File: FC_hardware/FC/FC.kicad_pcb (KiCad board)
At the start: 4 copper layers, 34 x 34 mm, 86 parts, among them J1 Pin_01x04, J10 GND, J11 GND, J12 GND, J13 530481410, J15 Pin_01x03, J16 PB2, J17 PC9, J18 PC8, J19 PB7, J2 USB4105GFA120, J20 PB6, J21 PA8, J22 PC11, J23 PC10, J24 PC12, J25 PB10, J26 PC7, J27 PC6, J3 530480810, J4 BAT, J5 5V, J6 5V, J7 3V3, J8 3V3, J9 GND, Q1 BC807W, U1 MP2348, U2 AMS1117-3.3, U3 STM32F446RETx, U4 MPU-9250, U5 DPS368XTSA1, U6 USBLC6-2SC6, Y1 ABM8G-25MHZ

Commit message: Dump pcb design
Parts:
- removed J17: PC9, footprints:1.27mm_pin
- removed J26: PC7, footprints:1.27mm_pin
- removed J27: PC6, footprints:1.27mm_pin
- removed J3: 530480810, footprints:MOLEX_530480810
- removed JP1: BOOT0, Jumper:SolderJumper-2_P1.3mm_Bridged_RoundedPad1.0x1.5mm
- added C23: 10nF, Capacitor_SMD:C_0603_1608Metric, F.Cu at (111.3, 108.5)
- added C24: 10uF, Capacitor_SMD:C_0603_1608Metric, F.Cu at (109.2, 104.5)
- added C25: 10uF, Capacitor_SMD:C_0603_1608Metric, F.Cu at (106.2, 104.5)
- added FB1: 120R, Inductor_SMD:L_1206_3216Metric, F.Cu at (108.2, 106.5)
- added J14: PB10, footprints:1.27mm_pin, F.Cu at (118.6, 129.2)
- C1, C2, C6, F1, J2, L1, Q1, R11, R13, R18, S1, U6: moved to B.Cu
- C10: value 6.8pF -> 47uF; footprint Capacitor_SMD:C_0603_1608Metric -> Capacitor_Tantalum_SMD:CP_EIA-3528-12_Kemet-T; moved to B.Cu
- C11, C12: value 0.1uF -> 6.8pF
- C15: value 0.1uF -> 1uF; footprint Capacitor_SMD:C_0603_1608Metric -> Capacitor_SMD:C_0805_2012Metric
- C3: value 6.8nF -> 47uF; footprint Capacitor_SMD:C_0603_1608Metric -> Capacitor_Tantalum_SMD:CP_EIA-3528-12_Kemet-T; moved to B.Cu
- C4, C5: value 47uF -> 0.1uF; footprint Capacitor_Tantalum_SMD:CP_EIA-3528-12_Kemet-T -> Capacitor_SMD:C_0603_1608Metric
- C7: value 1uF -> 0.1uF; footprint Capacitor_SMD:C_0805_2012Metric -> Capacitor_SMD:C_0603_1608Metric; moved to B.Cu
- C8: value 1uF -> 6.8nF; footprint Capacitor_SMD:C_0805_2012Metric -> Capacitor_SMD:C_0603_1608Metric; moved to B.Cu
- C9: value 6.8pF -> 1uF; footprint Capacitor_SMD:C_0603_1608Metric -> Capacitor_SMD:C_0805_2012Metric; moved to B.Cu
- D1: value B320 -> Power-Red; footprint Diode_SMD:D_SMA -> LED_SMD:LED_0805_2012Metric
- D2: value Power-Red -> Status-Green
- D3: value Status-Green -> B320; footprint LED_SMD:LED_0805_2012Metric -> Diode_SMD:D_SMA; moved to B.Cu
- H1, H2, H3, H4: footprint MountingHole:MountingHole_2.2mm_M2 -> MountingHole:MountingHole_3.2mm_M3
- J1: value Pin_01x04 -> Conn_01x14; footprint Connector_PinHeader_1.27mm:PinHeader_1x04_P1.27mm_Vertical -> Connector_JST:JST_SH_SM14B-SRSS-TB_1x14-1MP_P1.00mm_Horizontal
- J10: value GND -> BAT; footprint footprints:1.27mm_pin -> Connector_PinHeader_2.00mm:PinHeader_1x01_P2.00mm_Vertical
- J11, J12: value GND -> 5V
- J13: value 530481410 -> PC12; footprint footprints:MOLEX_530481410 -> footprints:1.27mm_pin
- J15: value Pin_01x03 -> PC7; footprint Connector_PinHeader_1.27mm:PinHeader_1x03_P1.27mm_Vertical -> footprints:1.27mm_pin
- J16: value PB2 -> PC6
- J18: value PC8 -> 3V3
- J19: value PB7 -> 3V3
- J20: value PB6 -> GND
- J21: value PA8 -> GND
- J22: value PC11 -> GND
- J23: value PC10 -> GND
- J24: value PC12 -> SM08B-SRSS-TB; footprint footprints:1.27mm_pin -> Connector_JST:JST_SH_SM08B-SRSS-TB_1x08-1MP_P1.00mm_Horizontal
- J25: value PB10 -> Conn_01x06; footprint footprints:1.27mm_pin -> Connector_PinHeader_1.27mm:PinHeader_1x06_P1.27mm_Vertical; moved to B.Cu
- J4: value BAT -> PA8
- J5: value 5V -> PB6
- J6: value 5V -> PB7
- J7: value 3V3 -> PC8
- J8: value 3V3 -> PC9
- J9: value GND -> PC9
- JP2: value ESC_TEL -> BOOT0; footprint Jumper:SolderJumper-2_P1.3mm_Open_RoundedPad1.0x1.5mm -> Jumper:SolderJumper-2_P1.3mm_Bridged_RoundedPad1.0x1.5mm; moved to B.Cu
- R1: value 40.2k -> 604k
- R10: value 1k -> 4.7k; moved to B.Cu
- R12: value 40.2k -> 4.7k; moved to B.Cu
- R14: value 1k -> 5.1k
- R15: value 4.7k -> 1k; moved to B.Cu
- R16: value 4.7k -> 40.2k
- R17: value 1k -> 4.7k
- R2: value 7.68k -> 1k
- R3: value 15k -> 20R; moved to B.Cu
- R4: value 20R -> 15k; moved to B.Cu
- R5: value 604k -> 40.2k; moved to B.Cu
- R6: value 4.7k -> 7.68k; moved to B.Cu
- R7: value 4.7k -> 5.1k
- R8: value 5.1k -> 1k
- R9: value 5.1k -> 4.7k; moved to B.Cu
- U1: value MP2348 -> AMS1117-3.3; footprint Package_TO_SOT_SMD:SOT-583-8 -> Package_TO_SOT_SMD:SOT-223-3_TabPin2; moved to B.Cu
- U2: value AMS1117-3.3 -> MPU-9250; footprint Package_TO_SOT_SMD:SOT-223-3_TabPin2 -> Sensor_Motion:InvenSense_QFN-24_3x3mm_P0.4mm
- U3: value STM32F446RETx -> MP2348; footprint Package_QFP:LQFP-64_10x10mm_P0.5mm -> Package_TO_SOT_SMD:SOT-583-8; moved to B.Cu
- U4: value MPU-9250 -> DPS368XTSA1; footprint Sensor_Motion:InvenSense_QFN-24_3x3mm_P0.4mm -> footprints:XDCR_DPS368XTSA1; moved to B.Cu
- U5: value DPS368XTSA1 -> STM32F446RETx; footprint footprints:XDCR_DPS368XTSA1 -> Package_QFP:LQFP-64_10x10mm_P0.5mm
- moved J13 90.0 mm to (117.3, 129.2)
- moved C19 83.3 mm to (117.1, 123.7)
- moved C3 82.0 mm to (116.7, 116.2), turned to 180 degrees
- moved R13 81.0 mm to (124.2, 116.5)
- moved C4 80.4 mm to (109.8, 127.2), turned to -90 degrees
- moved C17 78.1 mm to (120.2, 112.3), turned to 90 degrees
- moved S1 77.1 mm to (105.8, 127.6), turned to 180 degrees
- moved R15 76.6 mm to (115.9, 118.8)
- moved J1 74.7 mm to (127.0, 113.0), turned to 90 degrees
- moved C5 73.1 mm to (110.8, 124.3), turned to 180 degrees
- moved C18 73.0 mm to (118.4, 110.0), turned to 180 degrees
- moved R4 72.4 mm to (103.8, 110.3)
- moved R10 72.1 mm to (107.0, 124.8), turned to 180 degrees
- moved R5 69.0 mm to (110.0, 108.8), turned to -90 degrees
- moved C20 68.2 mm to (105.0, 113.2), turned to -90 degrees
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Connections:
- C10 pad 1: /OSC_OUT -> +5V
- C11 pad 2: +3V3 -> /RCC_OSC_IN
- C12 pad 1: +3V3 -> /RCC_OSC_OUT
- C13 pad 1: Net-(U4-REGOUT) -> +5V
- C14 pad 1: +5V -> +3V3
- C15 pad 2: +3V3 -> /VCAP_1
- C16 pad 1: /ADC_I -> GND
- C16 pad 2: GND -> +3V3
- C17 pad 1: /ADC_U -> GND
- C17 pad 2: GND -> +3V3
- C2 pad 1: +5V -> +3V3
- C21 pad 1: GND -> /VBAT_ADC
- C21 pad 2: +3V3 -> GND
- C22 pad 1: +3V3 -> /IBAT_ADC
- C3 pad 1: Net-(U1-SS) -> +3V3
- C4 pad 1: +5V -> +3V3
- C5 pad 1: +3V3 -> Net-(U2-REGOUT)
- C7 pad 1: +3V3 -> GND
- C7 pad 2: GND -> +3V3
- C8 pad 1: GND -> Net-(U3-SS)
- C8 pad 2: /VCAP_1 -> GND
- C9 pad 1: GND -> +5V
- C9 pad 2: /OSC_IN -> GND
- D1 pad 1: +5V -> Net-(D1-K)
- D1 pad 2: VBUS -> +3V3
- D2 pad 1: Net-(D2-K) -> GND
- D2 pad 2: +3V3 -> Net-(D2-A)
- D3 pad 1: Net-(D3-K) -> +5V
- D3 pad 2: /LED -> VBUS
- J1 pad 1: GND -> unconnected-(J1-Pin_1-Pad1)
- J1 pad 2: /SWCLK -> /GPS_TX
- J1 pad 3: /SWDIO -> /GPS_RX
- J1 pad 4: +3V3 -> Net-(J1-Pin_4)
- J10 pad 1: GND -> +BATT
- J11 pad 1: GND -> +5V
- J12 pad 1: GND -> +5V
- J13 pad 1: GND -> /GEN_I2C3_SDA
- J15 pad 1: GND -> /GEN_UART2_RX
- J16 pad 1: /GEN_MOSI -> /GEN_UART2_TX
- J18 pad 1: /TIM8_3 -> +3V3
- J19 pad 1: /TIM4_2 -> +3V3
- J20 pad 1: /TIM4_1 -> GND
- J21 pad 1: /TIM1_1 -> GND
- J22 pad 1: /GEN_MISO -> GND
- J23 pad 1: /GEN_SCK -> GND
- J24 pad 1: /GEN_SDA -> GND
- J25 pad 1: /GEN_SCL -> GND
- J4 pad 1: +BATT -> /GEN_TIM2_CH1
- J5 pad 1: +5V -> /GEN_TIM2_CH2
- J6 pad 1: +5V -> /GEN_TIM2_CH3
- J7 pad 1: +3V3 -> /GEN_TIM2_CH4
- J8 pad 1: +3V3 -> /GEN_TIM8_CH3
- J9 pad 1: GND -> /GEN_TIM10_CH1
- JP2 pad 1: /ESC_RX -> GND
- JP2 pad 2: /ESC_RX_MCU -> /BOOT
- R1 pad 1: +5V -> /BAT_VIN
- R1 pad 2: Net-(R1-Pad2) -> Net-(U3-EN)
- R10 pad 1: /ADC_I -> /NRST
- R10 pad 2: Net-(J3-CURR) -> +3V3
- R11 pad 1: GND -> +3V3
- R11 pad 2: /ADC_U -> /MAG_SDA
- R12 pad 1: +BATT -> /BOOT
- R12 pad 2: /ADC_U -> +3V3
- R13 pad 1: GND -> Net-(Q1-B)
- R13 pad 2: Net-(D2-K) -> Net-(J1-Pin_4)
- R14 pad 1: GND -> Net-(J2-CC2)
- R14 pad 2: Net-(D3-K) -> GND
- R15 pad 1: /MAG_SDA -> GND
- R15 pad 2: +3V3 -> /SBUS_RX
- R16 pad 1: /MAG_SCL -> +BATT
- R16 pad 2: +3V3 -> /VBAT_ADC
- R17 pad 2: /SBUS_RX -> /VBAT_ADC
- R18 pad 1: Net-(Q1-B) -> /IBAT_ADC
- R18 pad 2: Net-(J13-SBUS_RX) -> Net-(J24-Pad7)
- R2 pad 1: Net-(R1-Pad2) -> GND
- R2 pad 2: GND -> Net-(D1-K)
- R3 pad 1: Net-(U1-FB) -> Net-(U3-BST)
- R3 pad 2: Net-(R1-Pad2) -> Net-(C6-Pad1)
- R4 pad 1: Net-(U1-BST) -> Net-(U3-FB)
- R4 pad 2: Net-(C6-Pad1) -> Net-(R4-Pad2)
- R5 pad 1: /BAT_VIN -> +5V
- R5 pad 2: Net-(U1-EN) -> Net-(R4-Pad2)
- R6 pad 1: /NRST -> Net-(R4-Pad2)
- R6 pad 2: +3V3 -> GND
- R7 pad 1: /BOOT -> Net-(J2-CC1)
- R7 pad 2: +3V3 -> GND
- R8 pad 1: Net-(J2-CC2) -> /STATUS_LED
- R8 pad 2: GND -> Net-(D2-A)
- R9 pad 1: Net-(J2-CC1) -> /MAG_SCL
- R9 pad 2: GND -> +3V3
- U1 pad 1: unconnected-(U1-MODE-Pad1) -> GND
- U1 pad 2: /BAT_VIN -> +3V3
- U1 pad 3: /SW -> +5V
- U2 pad 1: GND -> +3V3
- U2 pad 2: +3V3 -> (no net)
- U2 pad 3: +5V -> (no net)
- U3 pad 1: +3V3 -> unconnected-(U3-MODE-Pad1)
- U3 pad 2: /BAR_CSB -> /BAT_VIN
- U3 pad 3: unconnected-(U3-PC14-Pad3) -> /SW
- U3 pad 4: unconnected-(U3-PC15-Pad4) -> GND
- U3 pad 5: /OSC_IN -> Net-(U3-BST)
- U3 pad 6: /OSC_OUT -> Net-(U3-EN)
- U3 pad 7: /NRST -> Net-(U3-SS)
- U3 pad 8: /ADC_I -> Net-(U3-FB)
- U4 pad 1: +3V3 -> GND
- U4 pad 2: (no net) -> /BAR_CS
- U4 pad 3: (no net) -> /IMU_BAR_MOSI
- U4 pad 4: (no net) -> /IMU_BAR_SCK
- U4 pad 5: (no net) -> /IMU_BAR_MISO
- U4 pad 6: (no net) -> +3V3
- U4 pad 7: unconnected-(U4-AUX_CL-Pad7) -> GND
- U5 pad 1: GND -> +3V3
- U5 pad 2: /BAR_CSB -> /LORA_IRQN
- U5 pad 3: /IMU_BAR_MOSI -> /LORA_RST
- U5 pad 4: /IMU_BAR_SCK -> unconnected-(U5-PC15-Pad4)
- U5 pad 5: /IMU_BAR_MISO -> /RCC_OSC_IN
- U5 pad 6: +3V3 -> /RCC_OSC_OUT
- U5 pad 7: GND -> /NRST
- U5 pad 8: +3V3 -> unconnected-(U5-PC0-Pad8)
- U6 pad 1: /USB_DP -> /USB_OTG_FS_DP
- U6 pad 3: /USB_DN -> /USB_OTG_FS_DN
- Y1 pad 1: /OSC_IN -> /RCC_OSC_IN
- Y1 pad 3: /OSC_OUT -> /RCC_OSC_OUT
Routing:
- net GND: track 0.00 -> 58.9 mm, vias 0 -> 48
- net /USB_OTG_FS_DP: track 0.00 -> 35.3 mm, vias 0 -> 1
- net /USB_OTG_FS_DN: track 0.00 -> 35.3 mm, vias 0 -> 1
- net +3V3: track 0.00 -> 28.1 mm, vias 0 -> 26
- net /NRST: track 0.00 -> 24.7 mm, vias 0 -> 1
- net +5V: track 0.00 -> 19.7 mm, vias 0 -> 2
- net +BATT: track 0.00 -> 18.0 mm, vias 0 -> 2
- net /GEN_TIM10_CH1: track 0.00 -> 17.8 mm, vias 0 -> 2
- net /GEN_TIM2_CH2: track 0.00 -> 17.7 mm, vias 0 -> 2
- net /STATUS_LED: track 0.00 -> 16.7 mm
- net /GEN_UART2_TX: track 0.00 -> 16.7 mm
- net /IBAT_ADC: track 0.00 -> 16.3 mm, vias 0 -> 1
- net /IMU_BAR_SCK: track 0.00 -> 16.1 mm, vias 0 -> 1
- net /GEN_TIM2_CH3: track 0.00 -> 15.4 mm, vias 0 -> 1
- net /GEN_UART2_RX: track 0.00 -> 15.3 mm, vias 0 -> 2
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- added copper zone on B.Cu, net +3V3
- added copper zone on In1.Cu, net +3V3
- added copper zone on B.Cu, net +5V
- added copper zone on B.Cu, net /SW
- added copper zone on B.Cu, net GND
- added copper zone on In2.Cu, net GND
- added copper zone on B.Cu, net VBUS
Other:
- board size 34 x 34 mm -> 35 x 35 mm

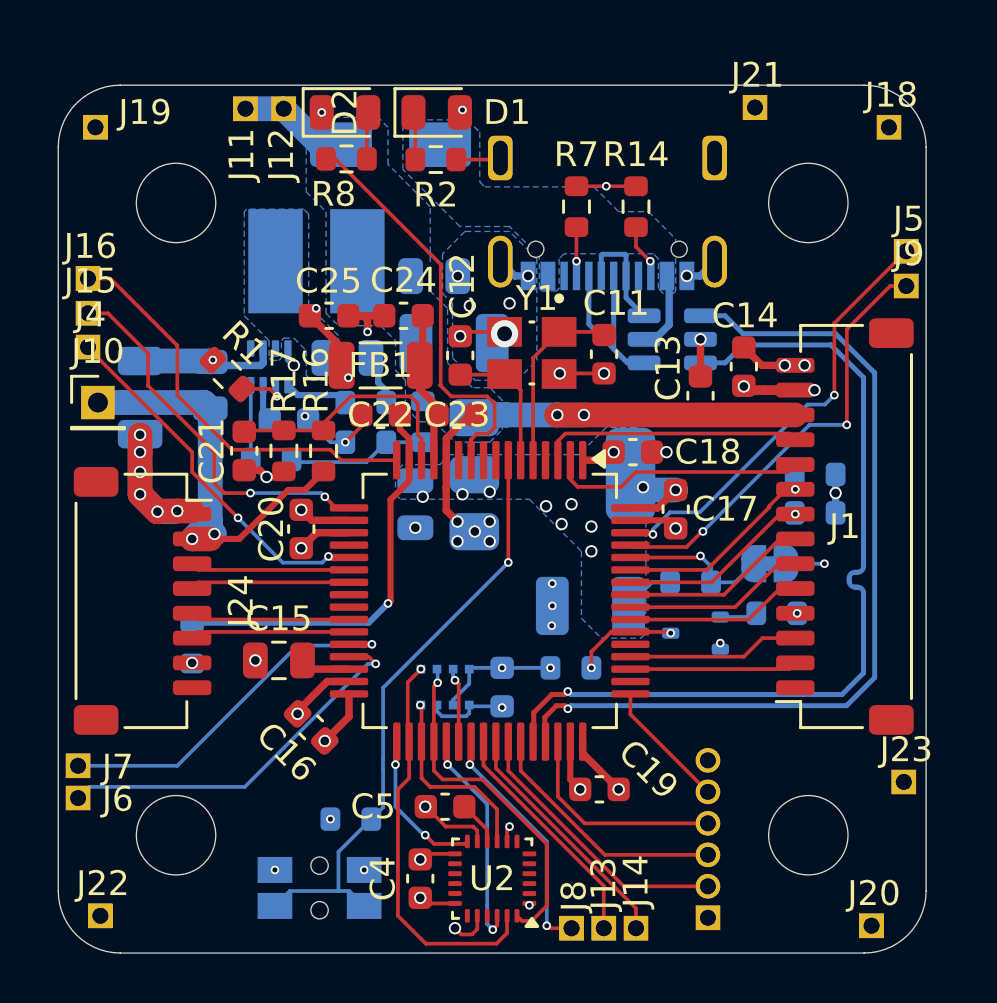
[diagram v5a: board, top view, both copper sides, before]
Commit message: min via hole d enlarged to 0.3mm and all vias resized accordingly
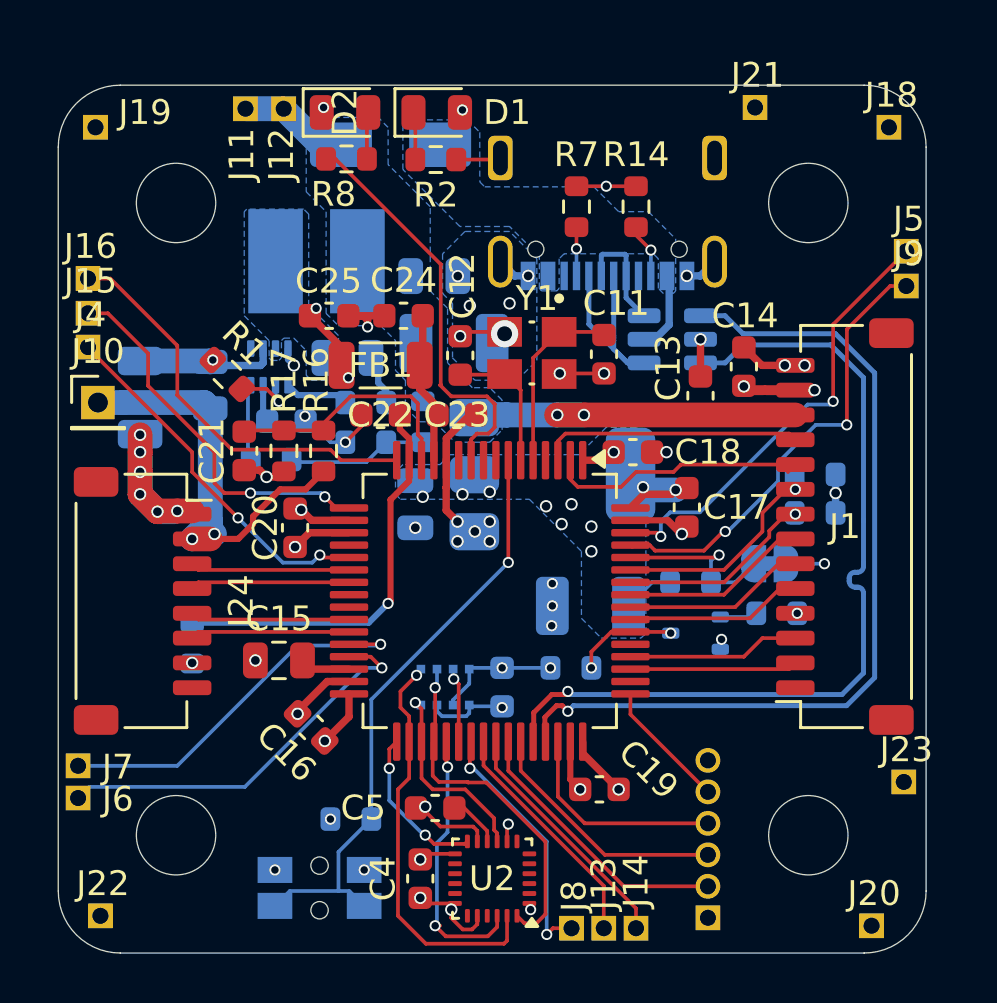
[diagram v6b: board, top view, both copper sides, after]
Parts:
- moved C17 0.46 mm to (120.6, 112.3)
- moved C5 0.40 mm to (110.5, 124.4)
- moved C20 0.25 mm to (104.8, 113.1)
- moved C8 0.11 mm to (104.5, 108.8)
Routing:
- net /IMU_CS: track 8.99 -> 11.1 mm
- net /BOOT: track 6.13 -> 6.95 mm
- net /GEN_TIM2_CH4: track 14.8 -> 15.5 mm
- net +3V3: track 28.1 -> 28.7 mm
- net /GEN_TIM10_CH1: track 17.8 -> 18.4 mm
- net GND: track 58.9 -> 59.6 mm

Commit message: Finalize design
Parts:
- removed J13: PC12, footprints:1.27mm_pin
- removed J14: PB10, footprints:1.27mm_pin
- removed J15: PC7, footprints:1.27mm_pin
- removed J16: PC6, footprints:1.27mm_pin
- removed J8: PC9, footprints:1.27mm_pin
- added J3: Conn_02x02_Counter_Clockwise, Connector_PinHeader_1.27mm:PinHeader_2x02_P1.27mm_Vertical, F.Cu at (116.5, 128.0)
- J25: footprint Connector_PinHeader_1.27mm:PinHeader_1x06_P1.27mm_Vertical -> Connector_PinHeader_1.27mm:PinHeader_2x03_P1.27mm_Vertical
- J4: value PA8 -> Conn_02x02_Counter_Clockwise; footprint footprints:1.27mm_pin -> Connector_PinHeader_1.27mm:PinHeader_2x02_P1.27mm_Vertical; moved to B.Cu
- moved J21 6.29 mm to (129.3, 98.0)
- moved J18 5.56 mm to (123.2, 96.2)
- moved J4 2.06 mm to (97.3, 104.0), turned to 90 degrees
- moved R10 1.74 mm to (105.8, 126.0)
- moved S1 0.93 mm to (105.8, 128.6)
- moved J25 0.91 mm to (122.3, 128.9), turned to 90 degrees
- moved R18 0.62 mm to (101.2, 118.0), turned to -135 degrees
- moved J5 0.30 mm to (129.4, 102.2)
- moved J9 0.20 mm to (129.4, 103.5)
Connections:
- J25 pad 2: /DEBUG_UART1_TX -> /SYS_JTCK-SWCLK
- J25 pad 3: /DEBUG_UART1_RX -> +3V3
- J25 pad 5: /SYS_JTCK-SWCLK -> /DEBUG_UART1_TX
- J25 pad 6: +3V3 -> /DEBUG_UART1_RX
- J4 pad 1: /GEN_TIM2_CH1 -> /GEN_UART2_RX
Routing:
- net /SYS_JTCK-SWCLK: track 5.24 -> 9.55 mm
- net +3V3: track 28.7 -> 32.4 mm, vias 26 -> 27
- net /GEN_TIM2_CH1: track 14.8 -> 16.9 mm
- net /GEN_I2C3_SCL: track 9.87 -> 8.22 mm
- net /GEN_I2C3_SDA: track 9.53 -> 7.90 mm
- net /SYS_JTMS-SWDIO: track 8.71 -> 9.81 mm
- net /IBAT_ADC: track 16.3 -> 15.3 mm
- net /NRST: track 24.7 -> 25.6 mm
- net /DEBUG_UART1_RX: track 10.1 -> 9.34 mm
- net /DEBUG_UART1_TX: track 11.2 -> 10.4 mm
- net /GEN_TIM8_CH3: track 10.3 -> 10.8 mm
- net GND: vias 48 -> 52
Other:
- board text added: ":P"
- board text added: "LEGO kör"
